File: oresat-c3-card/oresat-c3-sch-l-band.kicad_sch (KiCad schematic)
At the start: 69 parts, among them U15 Qorvo 856930, U16 AT86RF215, U17 SI4112-GM, U2 BP0805A1308, U23 NCS2-62+, U3 BP0805A1308, U4 BGB741L7ESD, U41 TQP3M9036, U5 BP0805A1308, U7 MAC-24+, X1 TXETALSANF-26.000000

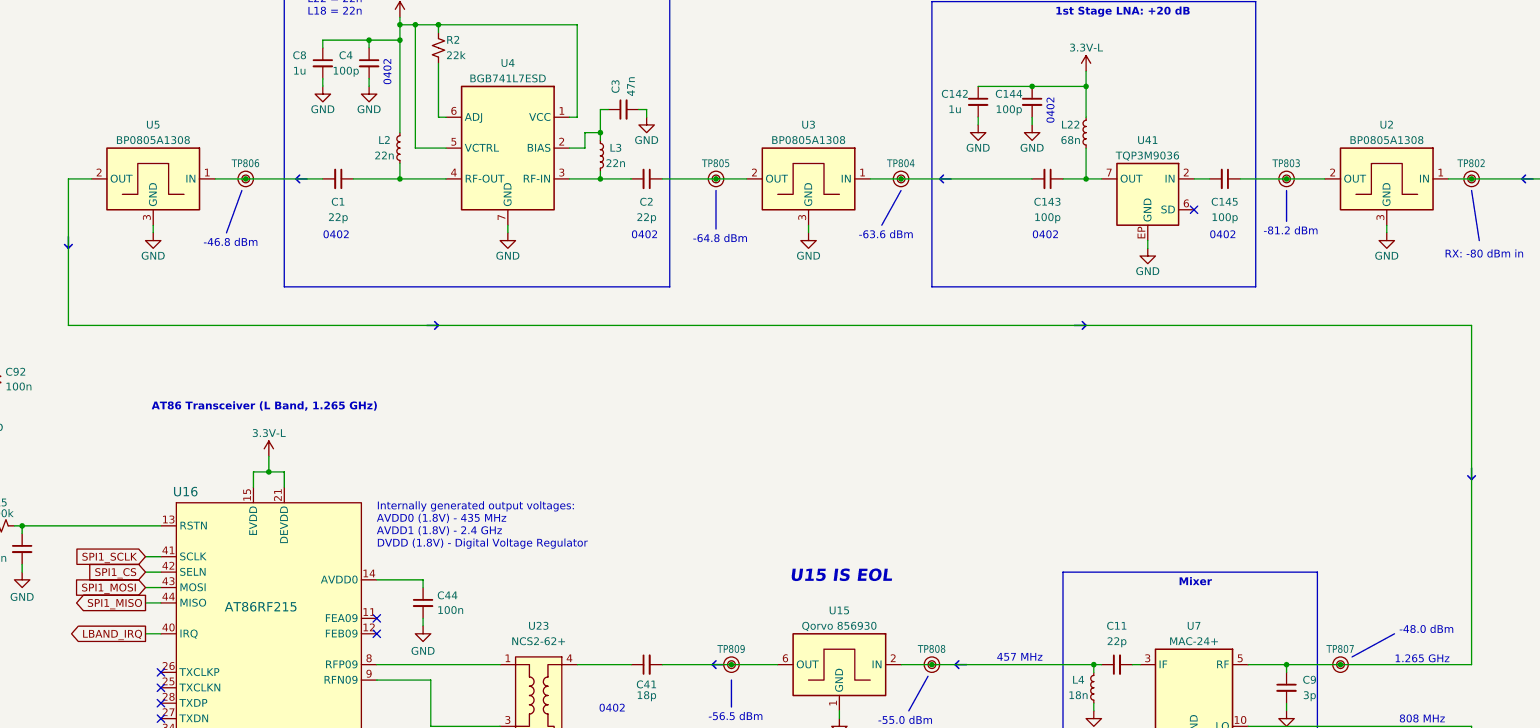
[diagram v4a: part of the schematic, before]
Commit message: BOM only change: Upgraded single gate inverter to AEC qualified version
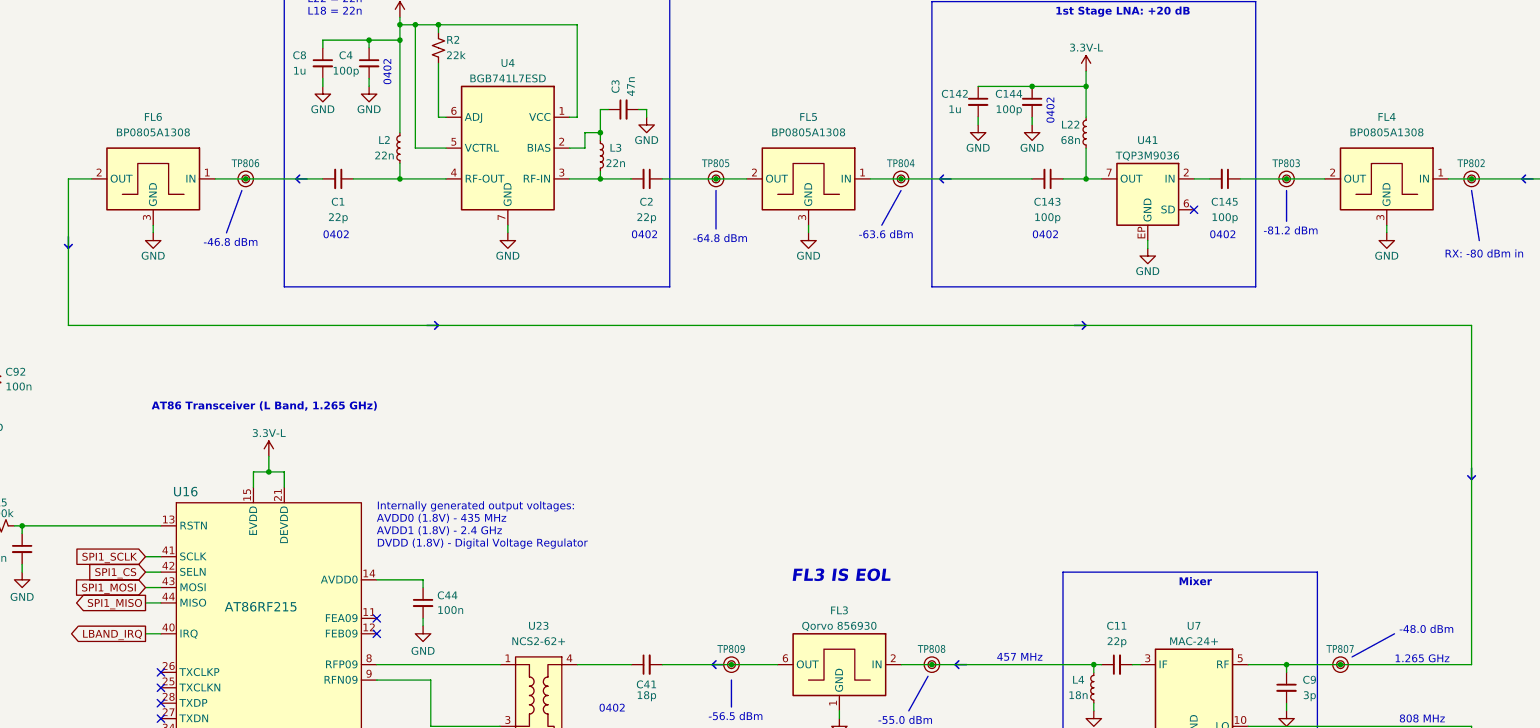
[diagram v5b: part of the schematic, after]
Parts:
- renumbered U15 to FL3, U2 to FL4, U3 to FL5, U5 to FL6
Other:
- note added: "FL3 IS EOL"
- note removed: "U15 IS EOL"
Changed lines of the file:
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@@
 		)
 	)
-	(text "U15 IS EOL"
+	(text "FL3 IS EOL"
 		(exclude_from_sim no)
 		(at 251.714 126.492 0)
@@
 		(dnp no)
 		(fields_autoplaced yes)
-		(property "Reference" "U2"
-			(at 341.63 52.07 0)
+		(property "Reference" "FL4"
+			(at 341.63 50.8 0)
 			(effects
 				(font
@@
 		)
 		(property "Value" "BP0805A1308"
-			(at 341.63 54.61 0)
+			(at 341.63 53.34 0)
 			(effects
 				(font
@@
 			(project "oresat-c3"
 				(path "/65d12cdd-c326-4033-9053-c59fa4e0b25e/1b68ea4b-cacf-4529-b1d4-9be5d7c1043c"
-					(reference "U2")
+					(reference "FL4")
 					(unit 1)
 				)
@@
 		(dnp no)
 		(fields_autoplaced yes)
-		(property "Reference" "U3"
-			(at 246.38 52.07 0)
+		(property "Reference" "FL5"
+			(at 246.38 50.8 0)
 			(effects
 				(font
@@
 		)
 		(property "Value" "BP0805A1308"
-			(at 246.38 54.61 0)
+			(at 246.38 53.34 0)
 			(effects
 				(font
@@
 			(project "oresat-c3"
 				(path "/65d12cdd-c326-4033-9053-c59fa4e0b25e/1b68ea4b-cacf-4529-b1d4-9be5d7c1043c"
-					(reference "U3")
+					(reference "FL5")
 					(unit 1)
 				)
@@
 		(dnp no)
 		(fields_autoplaced yes)
-		(property "Reference" "U5"
-			(at 138.43 52.07 0)
+		(property "Reference" "FL6"
+			(at 138.43 50.8 0)
 			(effects
 				(font
@@
 		)
 		(property "Value" "BP0805A1308"
-			(at 138.43 54.61 0)
+			(at 138.43 53.34 0)
 			(effects
 				(font
@@
 			(project "oresat-c3"
 				(path "/65d12cdd-c326-4033-9053-c59fa4e0b25e/1b68ea4b-cacf-4529-b1d4-9be5d7c1043c"
-					(reference "U5")
+					(reference "FL6")
 					(unit 1)
 				)
@@
 		(dnp no)
 		(fields_autoplaced yes)
-		(property "Reference" "U15"
+		(property "Reference" "FL3"
 			(at 251.46 132.08 0)
 			(effects
@@
 			(project "oresat-c3"
 				(path "/65d12cdd-c326-4033-9053-c59fa4e0b25e/1b68ea4b-cacf-4529-b1d4-9be5d7c1043c"
-					(reference "U15")
+					(reference "FL3")
 					(unit 1)
 				)

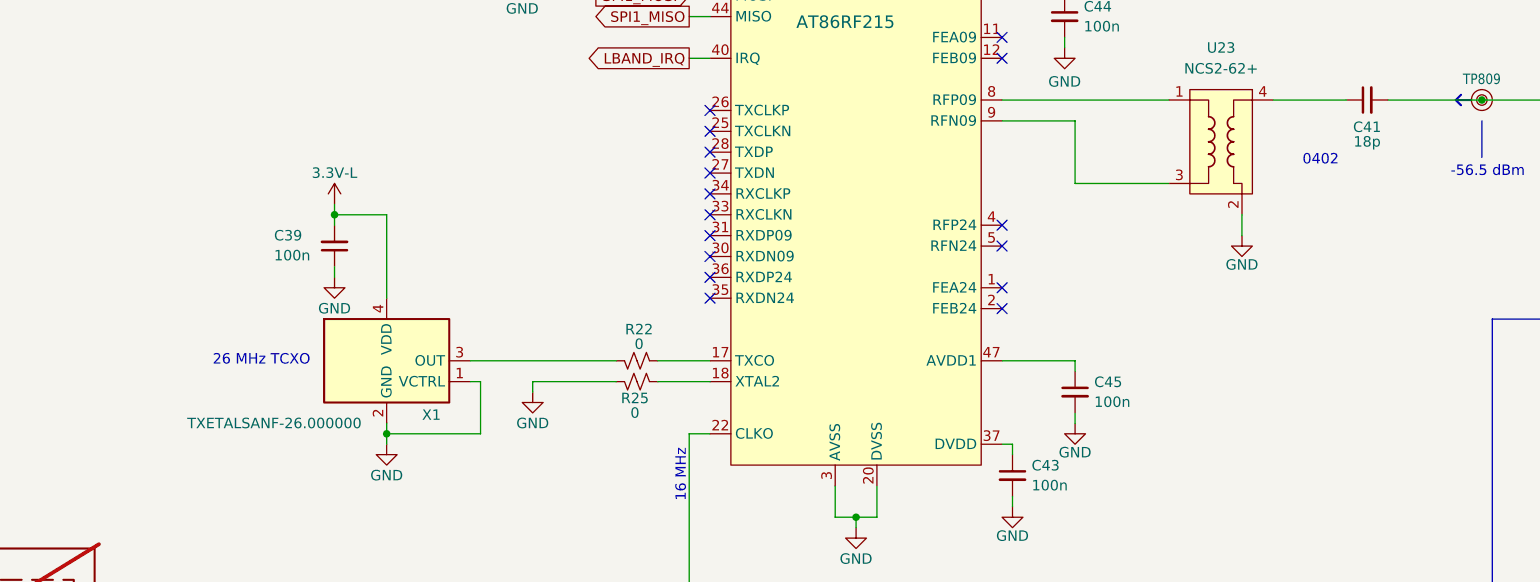
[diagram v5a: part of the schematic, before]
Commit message: Fix BOM errors given feedback from CM
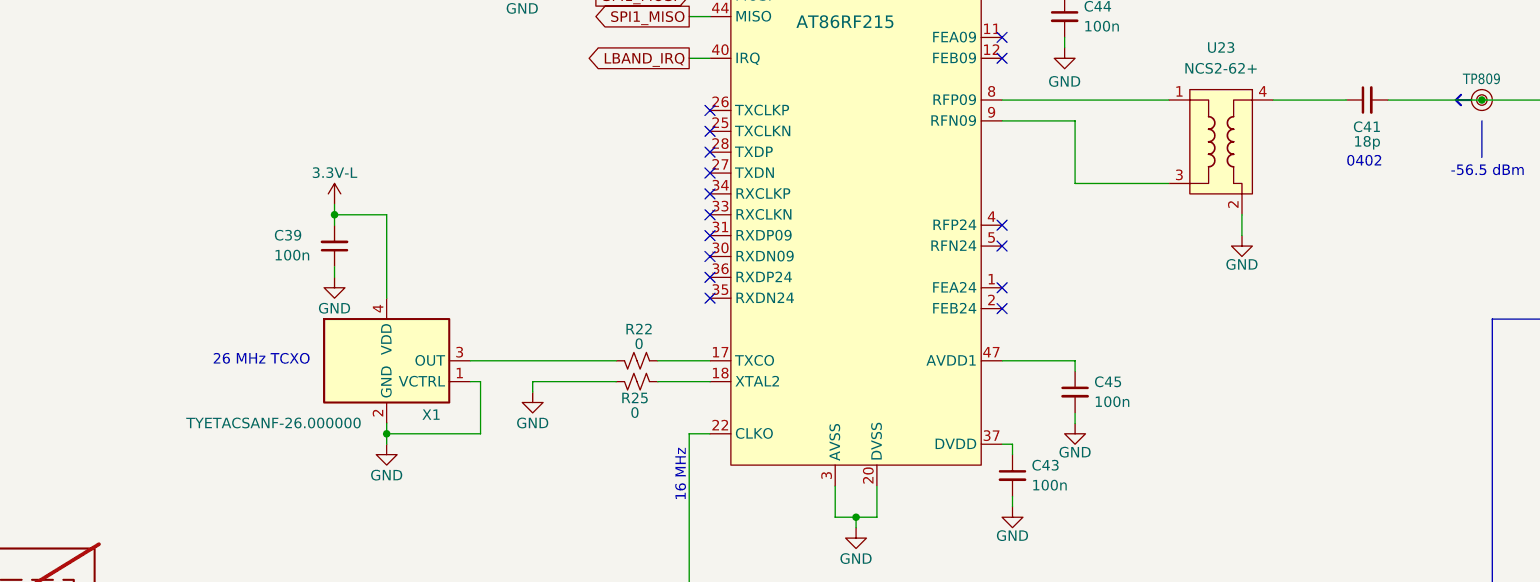
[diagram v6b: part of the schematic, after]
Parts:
- C1, C11, C2: DPN 399-15987-1-ND -> 399-CBR04C220J5GACAUTOCT-ND; MPN C0603C220J1GACAUTO -> CBR04C220J5GACAUTO
- C41: DPN 399-15952-1-ND -> 399-CBR04C180J5GACAUTOCT-ND; MPN C0402C180J5GACAUTO -> CBR04C180J5GACAUTO
- R6: MPN RMCF1206FT75R0 -> RMCF0603FT75R0
- X1: value TXETALSANF-26.000000 -> TYETACSANF-26.000000; DPN 1664-TXETALSANF-26.000000CT-ND -> 1664-TYETACSANF-26.000000CT-ND; MPN TXETALSANF-26.000000 -> TYETACSANF-26.000000
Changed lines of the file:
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@@
 	(text "0402"
 		(exclude_from_sim no)
-		(at 211.836 149.098 0)
+		(at 217.17 149.352 0)
 		(effects
 			(font
@@
 			)
 		)
-		(property "Datasheet" "~"
+		(property "Datasheet" "https://content.kemet.com/datasheets/KEM_C1121_CBR_AUTO.pdf"
 			(at 219.71 140.97 0)
 			(effects
@@
 			)
 		)
-		(property "Description" "18pF ±5% 50V Ceramic Capacitor C0G, NP0 0402 (1005 Metric)"
+		(property "Description" "18 pF ±5% 50V Ceramic Capacitor C0G, NP0 0402 (1005 Metric)"
 			(at 219.71 140.97 0)
 			(effects
@@
 			)
 		)
-		(property "DPN" "399-15952-1-ND"
+		(property "DPN" "399-CBR04C180J5GACAUTOCT-ND"
 			(at 219.71 140.97 0)
 			(effects
@@
 			)
 		)
-		(property "MPN" "C0402C180J5GACAUTO"
+		(property "MPN" "CBR04C180J5GACAUTO"
 			(at 219.71 140.97 0)
 			(effects
@@
 			)
 		)
-		(property "MPN" "RMCF1206FT75R0"
+		(property "MPN" "RMCF0603FT75R0"
 			(at 143.51 231.14 90)
 			(effects
@@
 			)
 		)
-		(property "Datasheet" "https://yageogroup.com/content/datasheet/asset/file/KEM_C1022_C0G_AUTO_SMD"
+		(property "Datasheet" "https://content.kemet.com/datasheets/KEM_C1121_CBR_AUTO.pdf"
 			(at 297.18 140.97 0)
 			(effects
@@
 			)
 		)
-		(property "Description" "22 pF ±5% 100V Ceramic Capacitor C0G, NP0 0603 (1608 Metric)"
+		(property "Description" "22 pF ±5% 50V Ceramic Capacitor C0G, NP0 0402 (1005 Metric)"
 			(at 297.18 140.97 0)
 			(effects
@@
 			)
 		)
-		(property "DPN" "399-15987-1-ND"
+		(property "DPN" "399-CBR04C220J5GACAUTOCT-ND"
 			(at 297.18 140.97 0)
 			(effects
@@
 			)
 		)
-		(property "MPN" "C0603C220J1GACAUTO"
+		(property "MPN" "CBR04C220J5GACAUTO"
 			(at 297.18 140.97 0)
 			(effects
@@
 			)
 		)
-		(property "Datasheet" "https://yageogroup.com/content/datasheet/asset/file/KEM_C1022_C0G_AUTO_SMD"
+		(property "Datasheet" "https://content.kemet.com/datasheets/KEM_C1121_CBR_AUTO.pdf"
 			(at 219.71 60.96 0)
 			(effects
@@
 			)
 		)
-		(property "Description" "22 pF ±5% 100V Ceramic Capacitor C0G, NP0 0603 (1608 Metric)"
+		(property "Description" "22 pF ±5% 50V Ceramic Capacitor C0G, NP0 0402 (1005 Metric)"
 			(at 219.71 60.96 0)
 			(effects
@@
 			)
 		)
-		(property "DPN" "399-15987-1-ND"
+		(property "DPN" "399-CBR04C220J5GACAUTOCT-ND"
 			(at 219.71 60.96 0)
 			(effects
@@
 			)
 		)
-		(property "MPN" "C0603C220J1GACAUTO"
+		(property "MPN" "CBR04C220J5GACAUTO"
 			(at 219.71 60.96 0)
 			(effects
@@
 			)
 		)
-		(property "Value" "TXETALSANF-26.000000"
+		(property "Value" "TYETACSANF-26.000000"
 			(at 97.282 180.34 0)
 			(effects
@@
 			)
 		)
-		(property "DPN" "1664-TXETALSANF-26.000000CT-ND"
+		(property "DPN" "1664-TYETACSANF-26.000000CT-ND"
 			(at 100.33 172.72 0)
 			(effects
@@
 			)
 		)
-		(property "MPN" "TXETALSANF-26.000000"
+		(property "MPN" "TYETACSANF-26.000000"
 			(at 100.33 172.72 0)
 			(effects
@@
 			)
 		)
-		(property "Datasheet" "https://yageogroup.com/content/datasheet/asset/file/KEM_C1022_C0G_AUTO_SMD"
+		(property "Datasheet" "https://content.kemet.com/datasheets/KEM_C1121_CBR_AUTO.pdf"
 			(at 168.91 60.96 0)
 			(effects
@@
 			)
 		)
-		(property "Description" "22 pF ±5% 100V Ceramic Capacitor C0G, NP0 0603 (1608 Metric)"
+		(property "Description" "22 pF ±5% 50V Ceramic Capacitor C0G, NP0 0402 (1005 Metric)"
 			(at 168.91 60.96 0)
 			(effects
@@
 			)
 		)
-		(property "DPN" "399-15987-1-ND"
+		(property "DPN" "399-CBR04C220J5GACAUTOCT-ND"
 			(at 168.91 60.96 0)
 			(effects
@@
 			)
 		)
-		(property "MPN" "C0603C220J1GACAUTO"
+		(property "MPN" "CBR04C220J5GACAUTO"
 			(at 168.91 60.96 0)
 			(effects

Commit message: Upgrade to KiCad 10, fix a few BOM entries, and we caught the first error! Go kicad 10.
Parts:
- TP801, TP802, TP803, TP804, TP805, TP806, TP807, TP808, TP809, TP811: value ~ -> (none)
